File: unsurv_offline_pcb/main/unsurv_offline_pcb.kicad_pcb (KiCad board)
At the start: 2 copper layers, 40 x 60 mm, 42 parts, among them CN1 DF12-20DP, J1 10103594-0001LF, J2 S2B-PH-SM4-TB_LF__SN_, J3 TXRX, Q1 VP0610T, Q2 UMH3N, SW1 SW_Push_Open_Dual, SW2 SW_Push_Open_Dual, U1 MCP73831-2-OT, U2 NCP59800, U3 APX803L20, U4 MPU-6050_NRND, U5 ESP32-WROOM-32, U6 CH340G

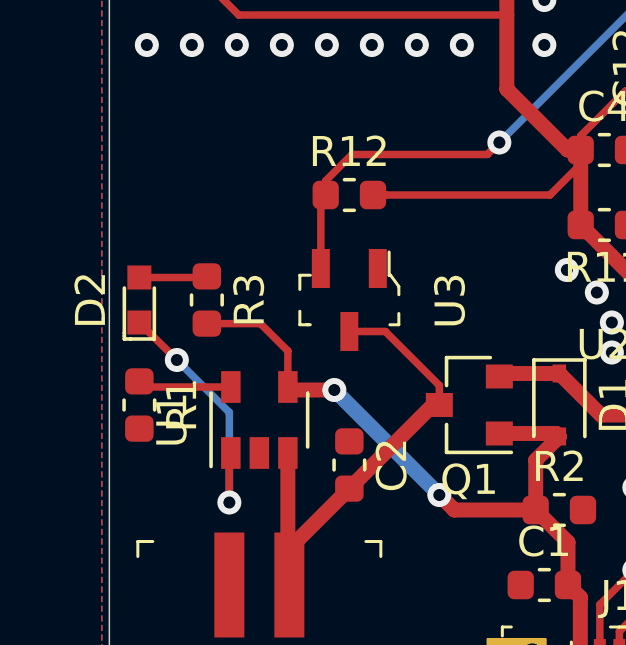
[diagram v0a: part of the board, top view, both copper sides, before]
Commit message: added DF40C-20 footprints
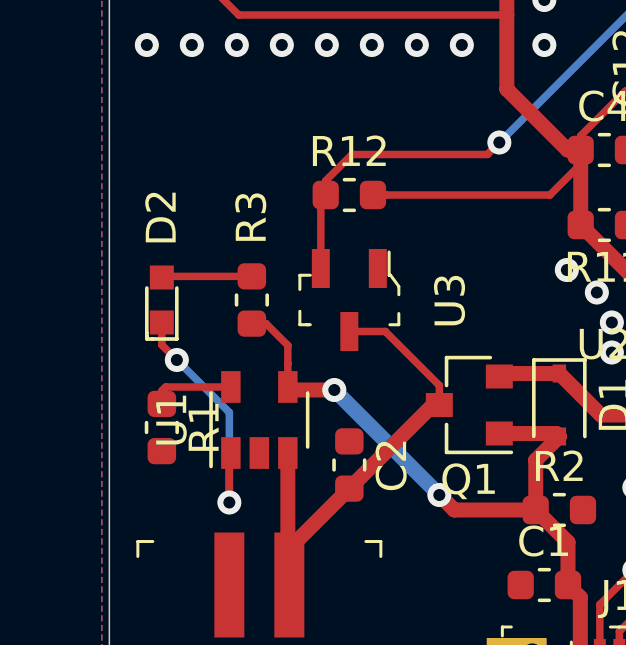
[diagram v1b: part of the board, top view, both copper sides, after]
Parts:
- moved R3 1.50 mm to (44.8, 82.5)
- moved R1 1.06 mm to (41.8, 86.8)
- moved D2 0.75 mm to (41.8, 82.5)
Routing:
- net +5V: track 24.8 -> 23.5 mm
- net Net-(D2-Pad2): track 2.27 -> 3.02 mm
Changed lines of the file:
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@@
     (thickness 1.6)
     (drawings 5)
-    (tracks 481)
+    (tracks 484)
     (zones 0)
     (modules 42)
@@
   )
   (module digikey-footprints:LED_0603 (layer F.Cu)
-    (at 41 82.5 90)
-    (attr smd)
-    (fp_text reference D2 (at 0 -1.61 90) (layer F.SilkS)
+    (at 41.75 82.5 90)
+    (attr smd)
+    (fp_text reference D2 (at 2.75 0 90) (layer F.SilkS)
       (effects (font (size 1 1) (thickness 0.15)))
     )
@@
   )
   (module Resistor_SMD:R_0603_1608Metric (layer F.Cu)
-    (at 41 86 270)
+    (at 41.75 86.75 270)
     (descr "Resistor SMD 0603 (1608 Metric), square (rectangular) end terminal, IPC_7351 nominal, (Body size source: http://www.tortai-tech.com/upload/download/2011102023233369053.pdf), generated with kicad-footprint-generator")
     (tags resistor)
@@
   )
   (module Resistor_SMD:R_0603_1608Metric (layer F.Cu)
-    (at 43.25 82.5 270)
+    (at 44.75 82.5 270)
     (descr "Resistor SMD 0603 (1608 Metric), square (rectangular) end terminal, IPC_7351 nominal, (Body size source: http://www.tortai-tech.com/upload/download/2011102023233369053.pdf), generated with kicad-footprint-generator")
     (tags resistor)
     (attr smd)
-    (fp_text reference R3 (at 0 -1.43 90) (layer F.SilkS)
+    (fp_text reference R3 (at -2.75 0 90) (layer F.SilkS)
       (effects (font (size 1 1) (thickness 0.15)))
     )
@@
   (segment (start 46.05 85.5) (end 45.95 85.4) (width 0.5) (layer F.Cu) (net 2))
   (segment (start 47.5 85.5) (end 46.05 85.5) (width 0.5) (layer F.Cu) (net 2))
-  (segment (start 45.95 85.4) (end 45.95 84.2) (width 0.25) (layer F.Cu) (net 2))
-  (segment (start 45.0375 83.2875) (end 43.25 83.2875) (width 0.25) (layer F.Cu) (net 2))
-  (segment (start 45.95 84.2) (end 45.0375 83.2875) (width 0.25) (layer F.Cu) (net 2))
+  (segment (start 45.95 84.62) (end 45.95 85.4) (width 0.25) (layer F.Cu) (net 2))
+  (segment (start 45.95 84.0125) (end 45.95 84.62) (width 0.25) (layer F.Cu) (net 2))
+  (segment (start 45.225 83.2875) (end 45.95 84.0125) (width 0.25) (layer F.Cu) (net 2))
+  (segment (start 44.75 83.2875) (end 45.225 83.2875) (width 0.25) (layer F.Cu) (net 2))
   (segment (start 46 90.7875) (end 48 88.7875) (width 0.5) (layer F.Cu) (net 3))
   (segment (start 46 92) (end 46 90.7875) (width 0.5) (layer F.Cu) (net 3))
@@
   (segment (start 47.434315 58.75) (end 48 58.75) (width 0.25) (layer F.Cu) (net 23))
   (segment (start 46.5 62.5) (end 46.5 59.684315) (width 0.25) (layer F.Cu) (net 23))
-  (via (at 49.25 57.5) (size 0.8) (drill 0.4) (layers F.Cu B.Cu) (net 23))
   (segment (start 50.4625 58.5) (end 50.25 58.5) (width 0.25) (layer F.Cu) (net 23))
   (segment (start 50.25 58.5) (end 49.25 57.5) (width 0.25) (layer F.Cu) (net 23))
+  (via (at 49.25 57.5) (size 0.8) (drill 0.4) (layers F.Cu B.Cu) (net 23) (status 1000000))
   (segment (start 53.1 84.95) (end 53 85.05) (width 0.5) (layer F.Cu) (net 26))
   (segment (start 55 84.95) (end 53.1 84.95) (width 0.5) (layer F.Cu) (net 26))
@@
   (segment (start 44 89.25) (end 44 86.25) (width 0.25) (layer B.Cu) (net 27))
   (segment (start 44 86.25) (end 42.25 84.5) (width 0.25) (layer B.Cu) (net 27))
-  (segment (start 42.25 84.5) (end 41 83.25) (width 0.25) (layer F.Cu) (net 27))
-  (segment (start 43.2125 81.75) (end 43.25 81.7125) (width 0.25) (layer F.Cu) (net 28))
-  (segment (start 41 81.75) (end 43.2125 81.75) (width 0.25) (layer F.Cu) (net 28))
+  (segment (start 41.75 84) (end 42.25 84.5) (width 0.25) (layer F.Cu) (net 27))
+  (segment (start 41.75 83.25) (end 41.75 84) (width 0.25) (layer F.Cu) (net 27))
+  (segment (start 41.7875 81.7125) (end 41.75 81.75) (width 0.25) (layer F.Cu) (net 28))
+  (segment (start 44.75 81.7125) (end 41.7875 81.7125) (width 0.25) (layer F.Cu) (net 28))
   (segment (start 59.9 97.325) (end 59.725 97.5) (width 0.25) (layer F.Cu) (net 29))
   (segment (start 59.9 94.47) (end 59.9 97.325) (width 0.25) (layer F.Cu) (net 29))
@@
   (segment (start 44.5 42.75) (end 44.5 41.5) (width 0.25) (layer F.Cu) (net 37))
   (segment (start 49 47.25) (end 44.5 42.75) (width 0.25) (layer F.Cu) (net 37))
-  (segment (start 41.1875 85.4) (end 41 85.2125) (width 0.25) (layer F.Cu) (net 38))
-  (segment (start 44.05 85.4) (end 41.1875 85.4) (width 0.25) (layer F.Cu) (net 38))
+  (segment (start 41.75 85.525) (end 41.75 85.9625) (width 0.25) (layer F.Cu) (net 38))
+  (segment (start 41.875 85.4) (end 41.75 85.525) (width 0.25) (layer F.Cu) (net 38))
+  (segment (start 44.05 85.4) (end 41.875 85.4) (width 0.25) (layer F.Cu) (net 38))
   (segment (start 50 49.9625) (end 48.9625 51) (width 0.25) (layer F.Cu) (net 39))
   (segment (start 50 48.5) (end 50 49.9625) (width 0.25) (layer F.Cu) (net 39))

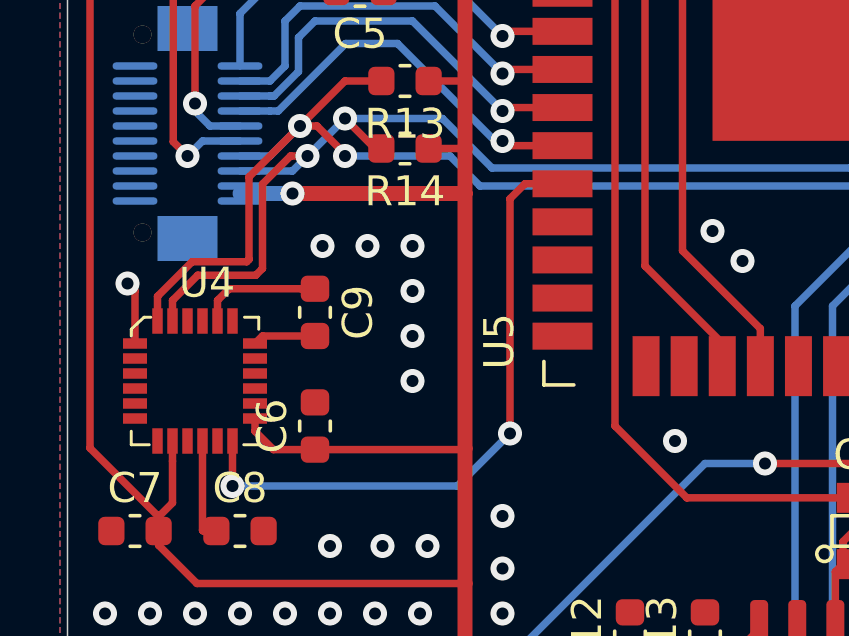
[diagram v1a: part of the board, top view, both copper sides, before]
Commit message: added power switch for GPS
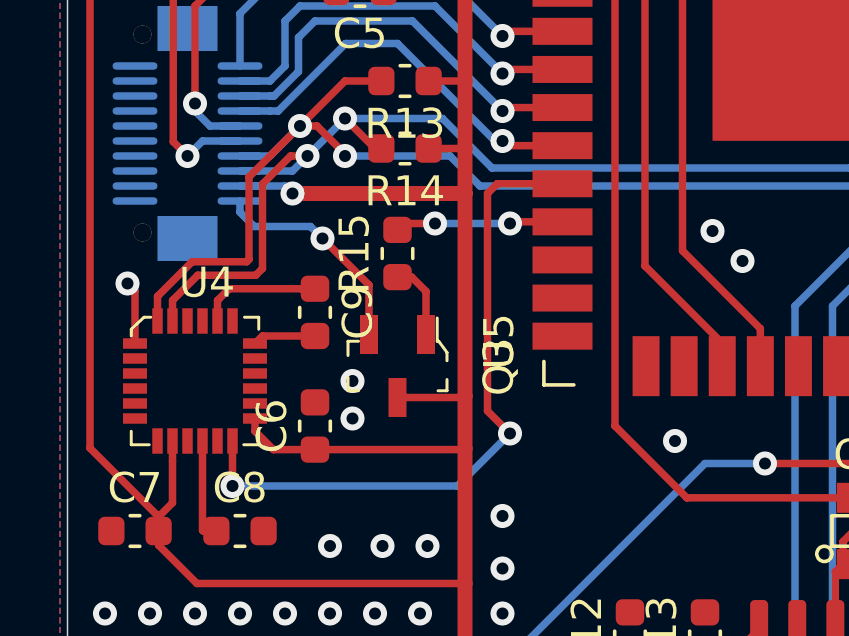
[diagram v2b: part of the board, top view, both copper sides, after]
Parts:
- added Q3: MMBT2907A-7-F, digikey-footprints:SOT-23-3, F.Cu at (51.0, 65.8)
- added R15: 600, Resistor_SMD:R_0603_1608Metric, F.Cu at (51.0, 62.0)
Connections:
- CN1 pad 10: +3V3 -> GPS3v3
- U5 pad 11: Net-(U5-Pad11) -> GPS_PWR
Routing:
- net GPS3v3: track 0.00 -> 7.33 mm, vias 0 -> 1
- net GPS_PWR: track 0.00 -> 5.61 mm, vias 0 -> 2
- net Net-(Q3-Pad1): track 0.00 -> 2.58 mm
- net +3V3: track 162.0 -> 164.4 mm
- net ACC_INT: track 21.3 -> 22.4 mm
- net GND: vias 44 -> 40

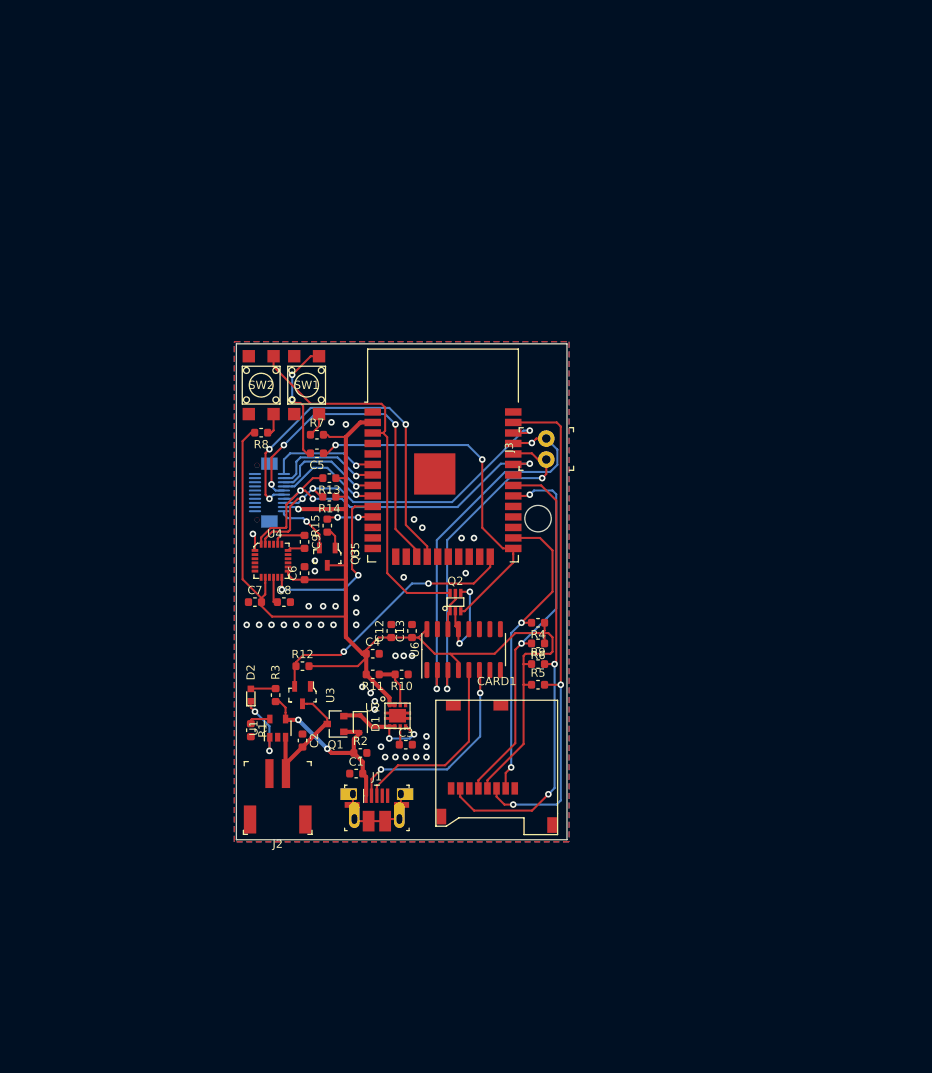
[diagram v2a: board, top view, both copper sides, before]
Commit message: reducing pcb size
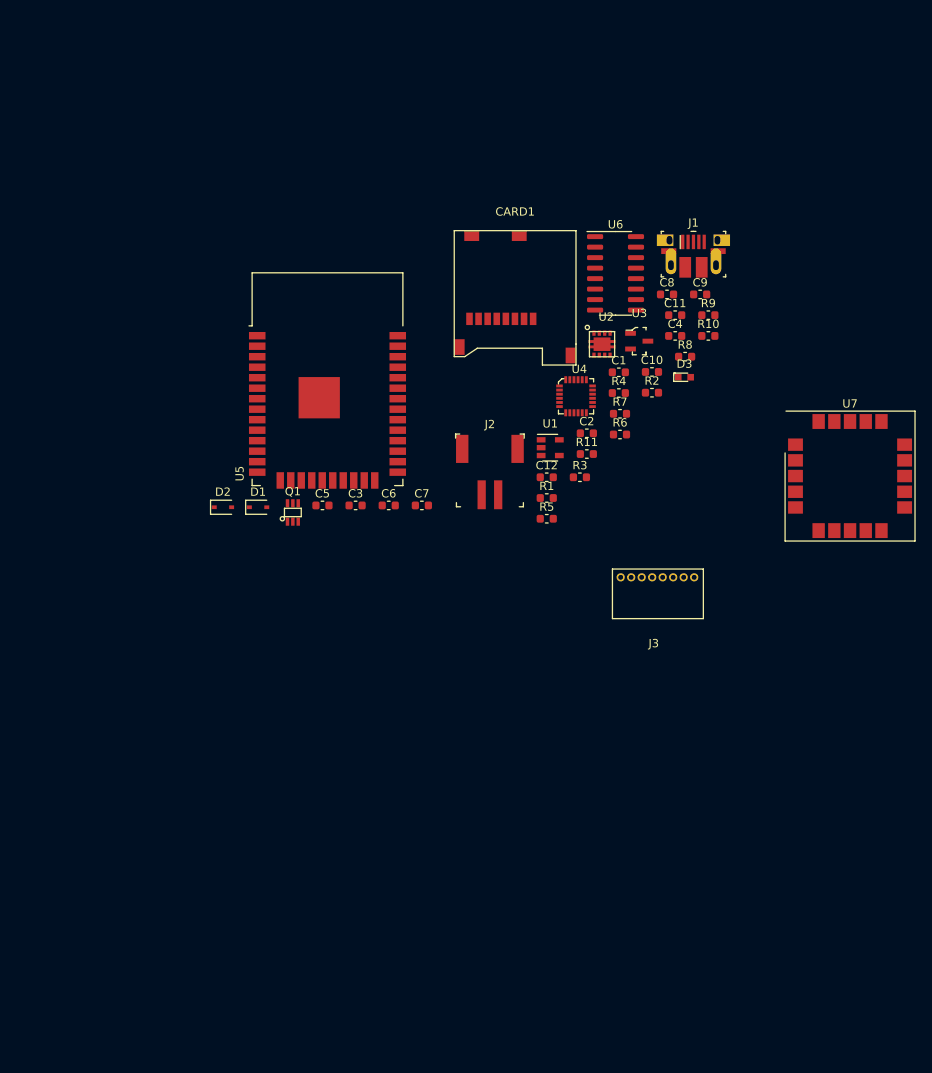
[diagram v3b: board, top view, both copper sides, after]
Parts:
- removed C13: 10yF, Capacitor_SMD:C_0603_1608Metric
- removed CN1: DF12-20DP, unsurv_offline_footprints:DF-12-20DP
- removed Q2: UMH3N, unsurv_offline_footprints:UMH3N
- removed Q3: MMBT2907A-7-F, digikey-footprints:SOT-23-3
- removed R12: 100k, Resistor_SMD:R_0603_1608Metric
- removed R13, R14: 4.7k, Resistor_SMD:R_0603_1608Metric
- removed R15: 600, Resistor_SMD:R_0603_1608Metric
- removed SW1, SW2: SW_Push_Open_Dual, unsurv_offline_footprints:2x2 Switch
- added C10: 2.2nF, Capacitor_SMD:C_0603_1608Metric, F.Cu at (90.3, 43.4)
- added C11: 100nF, Capacitor_SMD:C_0603_1608Metric, F.Cu at (93.1, 36.5)
- added D3: LED, digikey-footprints:LED_0603, F.Cu at (94.2, 44.0)
- added U7: ublox_SAM-M8Q, RF_GPS:ublox_SAM-M8Q, F.Cu at (114.2, 56.0)
- C12: value 100nF -> 10yF
- C2: value 4.7yF -> 100nF
- C3: value 10nF -> 1yF
- C5: value DNP -> 10nF
- C6: value 0.1yF -> 4.7yF
- C7: value 10nF -> 0.1yF
- C8: value 0.1yF -> 10nF
- C9: value 2.2nF -> 0.1yF
- CARD1: footprint unsurv_offline_footprints:TF-SMD_TF-101B -> unsurv_offline_pcb_footprints:TF-SMD_TF-101B
- D2: value LED -> D_Schottky; footprint digikey-footprints:LED_0603 -> Diode_SMD:D_SOD-323
- J3: value TXRX -> 1.27mm_female_connector; footprint digikey-footprints:PinHeader_1x2_P2.54mm_Drill1.02mm -> unsurv_offline_pcb_footprints:LPPB081NGCN-RC
- Q1: value VP0610T -> UMH3N; footprint Package_TO_SOT_SMD:SOT-23 -> unsurv_offline_pcb_footprints:UMH3N
- R10: value 10k -> 4.7k
- R11: value 30.9k -> 4.7k
- R2: value 100k -> 1k
- R3: value 1k -> 10k
- R8: value 10k -> 30.9k
- R9: value 10k -> 100k
- U2: footprint unsurv_offline_footprints:NCP59800 -> unsurv_offline_pcb_footprints:NCP59800
- moved J1 77.2 mm to (95.3, 30.5)
- moved C8 59.5 mm to (92.1, 34.0)
- moved U3 59.1 mm to (88.7, 39.7), turned to 0 degrees
- moved C1 58.0 mm to (86.3, 43.4)
- moved CARD1 56.9 mm to (73.7, 34.2)
- moved C9 56.5 mm to (96.1, 34.0), turned to 0 degrees
- moved R2 56.1 mm to (90.3, 45.9)
- moved R10 55.3 mm to (97.1, 39.0), turned to 0 degrees
- moved C4 53.1 mm to (93.1, 39.0)
- moved R8 52.1 mm to (94.3, 41.6), turned to 0 degrees
- moved U2 51.3 mm to (84.2, 40.0)
- moved C2 50.7 mm to (82.4, 50.8), turned to 0 degrees
- moved U6 49.1 mm to (85.9, 31.5), turned to 0 degrees
- moved U1 47.3 mm to (78.0, 52.6), turned to 0 degrees
- moved R9 47.0 mm to (97.1, 36.5)
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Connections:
- C2 pad 1: GND -> Net-(C2-Pad1)
- C2 pad 2: +BATT -> GND
- C3 pad 1: Net-(C3-Pad1) -> Net-(C2-Pad1)
- C4 pad 1: +3V3 -> GND
- C4 pad 2: GND -> +BATT
- C5 pad 1: 0 -> Net-(C5-Pad1)
- C5 pad 2: Net-(C5-Pad2) -> GND
- C7 pad 1: GND -> +3V3
- C7 pad 2: +3V3 -> GND
- C8 pad 1: Net-(C8-Pad1) -> GND
- C8 pad 2: GND -> +3V3
- D1 pad 1: Net-(D1-Pad1) -> Net-(C2-Pad1)
- D2 pad 1: Net-(D2-Pad1) -> Net-(C2-Pad1)
- D2 pad 2: Net-(D2-Pad2) -> +BATT
- J3 pad 1: RX0 -> +3V3
- J3 pad 2: TX0 -> GND
- Q1 pad 1: +5V -> RTS
- Q1 pad 2: Net-(D1-Pad1) -> DTR
- Q1 pad 3: +BATT -> 0
- R10 pad 1: GND -> +3V3
- R10 pad 2: Net-(R10-Pad2) -> SDA
- R11 pad 1: Net-(R10-Pad2) -> +3V3
- R11 pad 2: +3V3 -> SCL
- R2 pad 1: +5V -> Net-(D3-Pad2)
- R2 pad 2: GND -> +5V
- R3 pad 1: Net-(D2-Pad2) -> +3V3
- R3 pad 2: +5V -> 4
- R4 pad 2: 4 -> 23
- R5 pad 2: 23 -> 18
- R6 pad 2: 18 -> 19
- R7 pad 1: Net-(R7-Pad1) -> GND
- R7 pad 2: +3V3 -> Net-(R7-Pad2)
- R8 pad 1: Net-(R8-Pad1) -> Net-(R7-Pad2)
- R9 pad 1: +3V3 -> BATTALARM
- R9 pad 2: 19 -> +3V3
- U1 pad 1: Net-(D2-Pad1) -> Net-(D3-Pad1)
- U2 pad 3: Net-(R10-Pad2) -> Net-(R7-Pad2)
- U2 pad 5: Net-(D1-Pad1) -> Net-(C2-Pad1)
- U2 pad 6: Net-(C3-Pad1) -> Net-(C5-Pad1)
- U2 pad 7: Net-(D1-Pad1) -> Net-(C2-Pad1)
- U2 pad 8: Net-(D1-Pad1) -> Net-(C2-Pad1)
- U4 pad 10: Net-(C8-Pad1) -> Net-(C9-Pad1)
- U4 pad 20: Net-(C9-Pad1) -> Net-(C10-Pad1)
- U5 pad 11: GPS_PWR -> Net-(U5-Pad11)
- U5 pad 13: Net-(U5-Pad13) -> 14
- U5 pad 14: Net-(U5-Pad14) -> 12
- U5 pad 16: Net-(U5-Pad16) -> 13
- U5 pad 17: RX1 -> Net-(U5-Pad17)
- U5 pad 18: TX1 -> Net-(U5-Pad18)
- U5 pad 23: Net-(U5-Pad23) -> 15
- U5 pad 27: Net-(U5-Pad27) -> 16
- U5 pad 28: Net-(U5-Pad28) -> 17
- U5 pad 6: 34 -> Net-(U5-Pad6)
- U5 pad 7: 35 -> Net-(U5-Pad7)
- U5 pad 8: 32 -> Net-(U5-Pad8)
- U5 pad 9: GRST -> Net-(U5-Pad9)
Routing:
- net +3V3: track 164.4 -> 0.00 mm, vias 1 -> 0
- net 23: track 62.5 -> 0.00 mm, vias 2 -> 0
- net 19: track 56.3 -> 0.00 mm, vias 2 -> 0
- net SDA: track 48.2 -> 0.00 mm, vias 3 -> 0
- net SCL: track 47.3 -> 0.00 mm, vias 3 -> 0
- net EN: track 47.0 -> 0.00 mm
- net TX0: track 46.7 -> 0.00 mm, vias 2 -> 0
- net 18: track 46.4 -> 0.00 mm, vias 2 -> 0
- net TX1: track 44.8 -> 0.00 mm, vias 3 -> 0
- net 0: track 43.9 -> 0.00 mm, vias 2 -> 0
- net RX0: track 41.8 -> 0.00 mm, vias 2 -> 0
- net RX1: track 40.0 -> 0.00 mm, vias 3 -> 0
- net 4: track 37.8 -> 0.00 mm, vias 2 -> 0
- net BATTALARM: track 32.5 -> 0.00 mm, vias 2 -> 0
- net D-: track 25.4 -> 0.00 mm, vias 2 -> 0
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- removed copper zone on B.Cu, net GND
- removed copper zone on F.Cu, net GND
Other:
- board outline removed

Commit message: placing components on small pcb
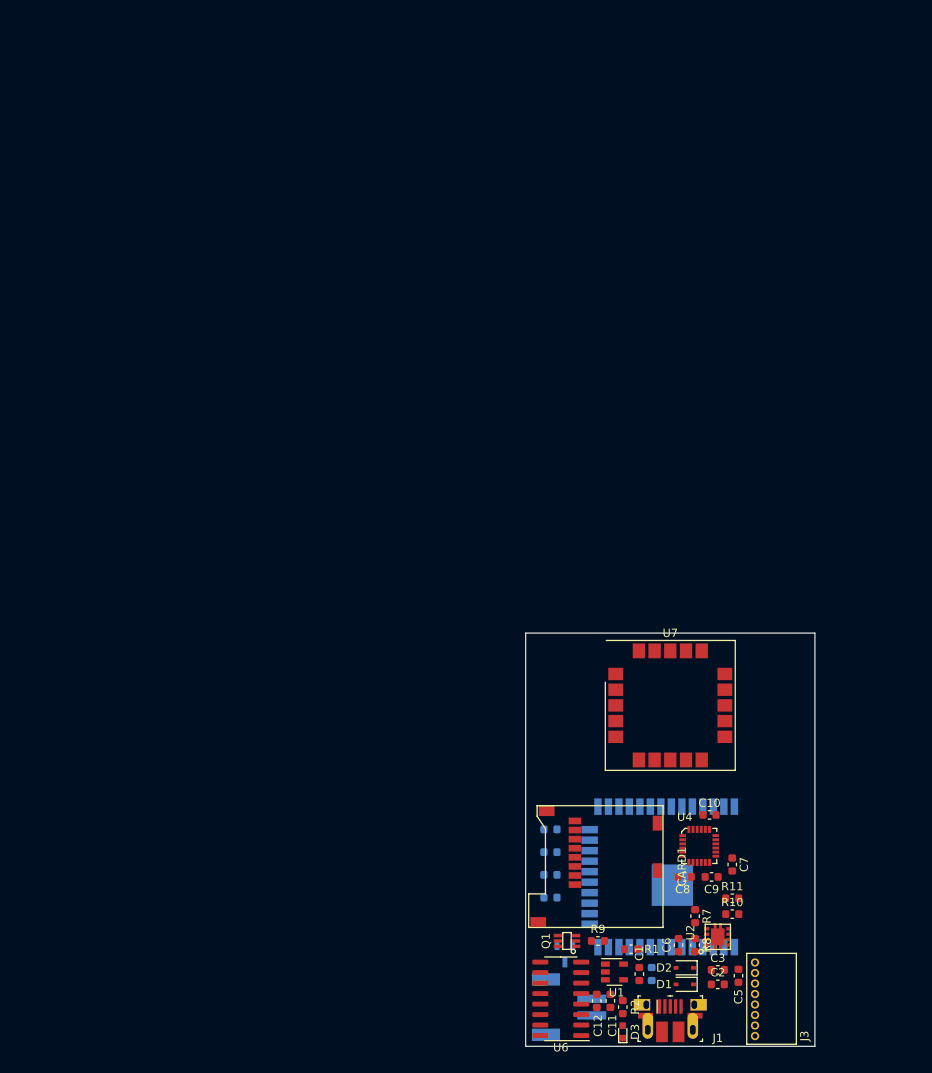
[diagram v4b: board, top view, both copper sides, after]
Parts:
- C4, J2, R3, R4, R5, R6, U3, U5: moved to B.Cu
- moved J1 92.5 mm to (92.5, 123.0)
- moved U6 88.0 mm to (79.2, 119.2), turned to 180 degrees
- moved C11 83.3 mm to (85.2, 119.5), turned to 270 degrees
- moved D3 79.6 mm to (86.8, 123.2), turned to 90 degrees
- moved D2 78.9 mm to (94.2, 115.5), turned to 180 degrees
- moved D1 77.4 mm to (94.2, 117.5), turned to 180 degrees
- moved C4 77.3 mm to (90.2, 116.2), turned to 90 degrees
- moved R9 76.9 mm to (83.8, 112.2)
- moved C5 76.0 mm to (100.8, 116.5), turned to 270 degrees
- moved U3 74.6 mm to (79.8, 113.8), turned to 270 degrees
- moved R2 74.4 mm to (86.8, 120.2), turned to 90 degrees
- moved U2 73.1 mm to (98.2, 111.8), turned to 90 degrees
- moved C1 72.8 mm to (88.8, 116.2), turned to 270 degrees
- moved C3 71.3 mm to (98.2, 115.8)
- moved R8 71.2 mm to (95.5, 112.8), turned to 270 degrees
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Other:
- board outline added: 35 x 50 mm
